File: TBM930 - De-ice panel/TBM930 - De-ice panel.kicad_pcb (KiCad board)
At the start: 2 copper layers, 190.5 x 101.6 mm, 79 parts, among them J1 SW_AIRFRAME_DE_ICE, J10 AVR-ISP-6, J2 SW_ICE_LIGHT, J3 SW_PROP_DE_ICE, J4 SW_WIND_SHIELD, J5 SW_PITOT_L_HTR, J6 SW_PITOT_R_HTR, J7 SW_INERT_SEP, J8 Barrel_Jack, J9 USB_B_Micro, SW1 SW_Push, SW2 SW_Push, U1 TLC5917IN, U2 TLC5917IN, U3 ATmega32U4-MU, Y1 Crystal_GND24

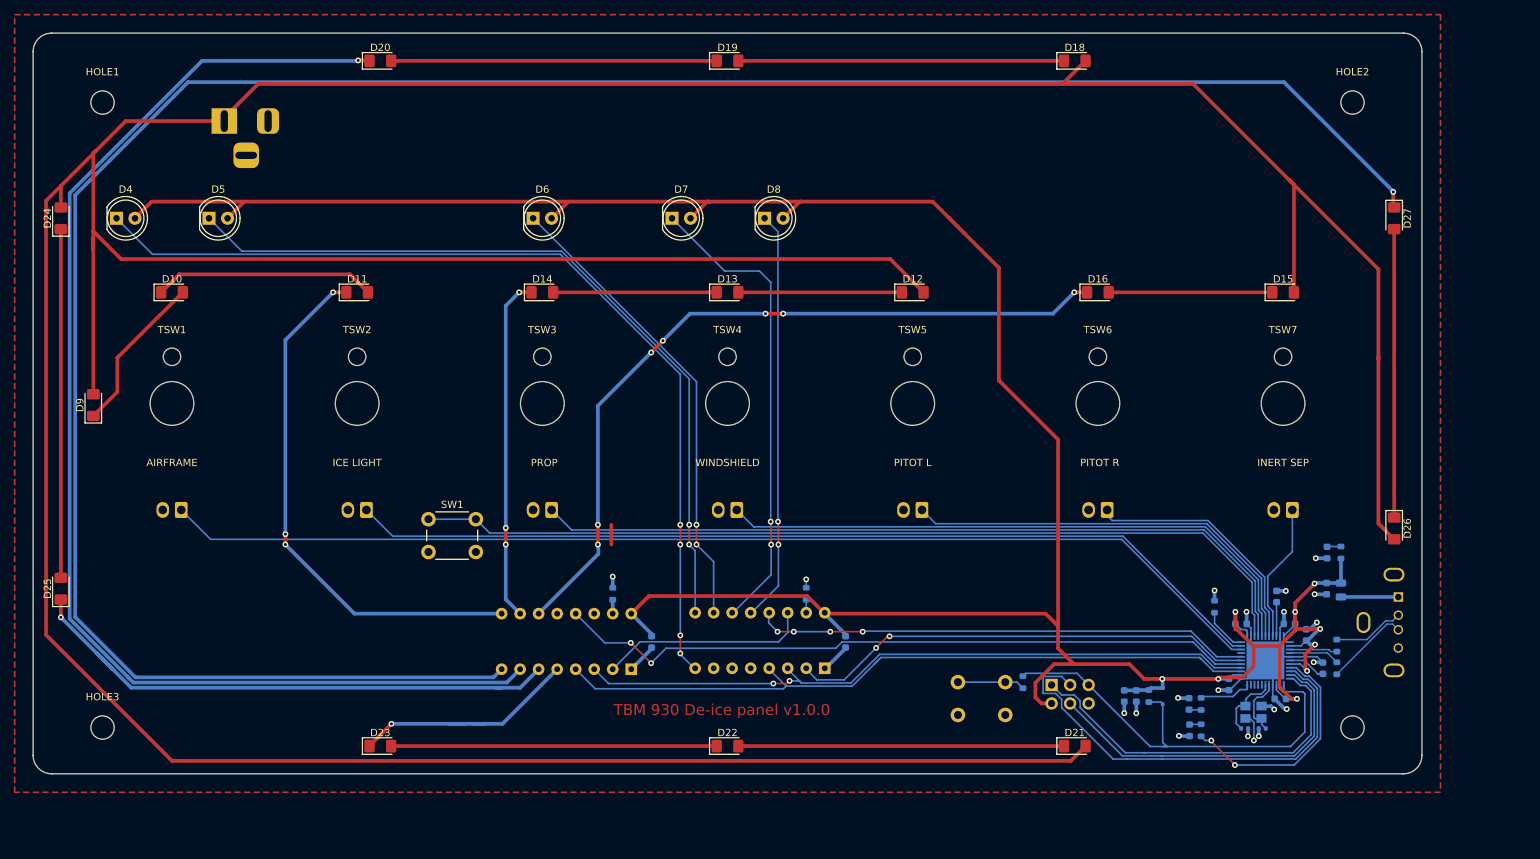
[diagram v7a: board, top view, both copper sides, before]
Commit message: Massive PCB reroute
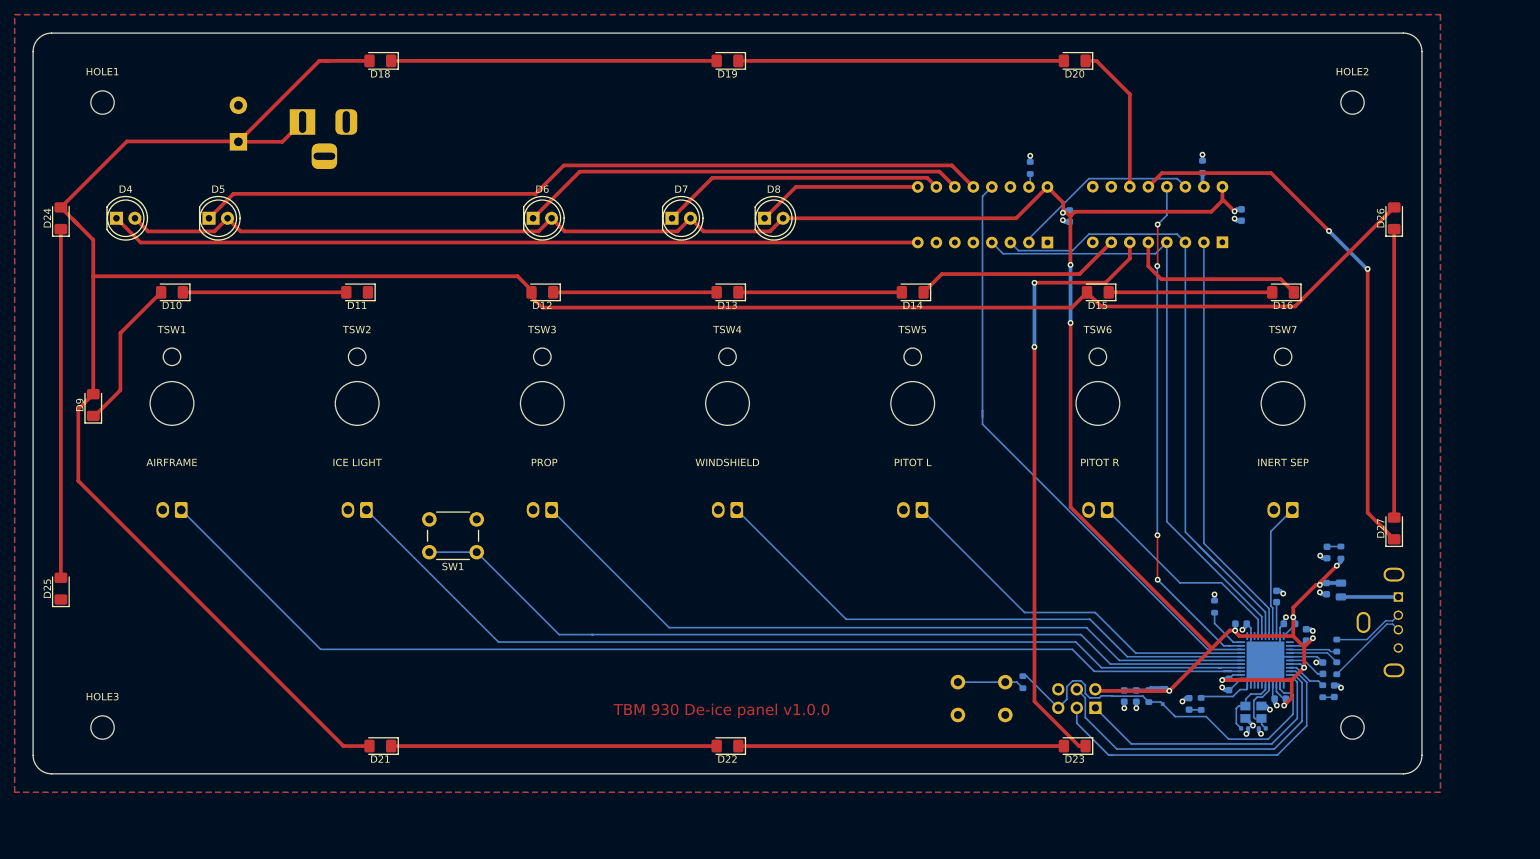
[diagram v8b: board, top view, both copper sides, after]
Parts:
- added J11: Screw_Terminal_01x02, TerminalBlock_Philmore:TerminalBlock_Philmore_TB132_1x02_P5.00mm_Horizontal, B.Cu at (67.5, 57.5)
- moved U1 100.0 mm to (202.5, 71.2)
- moved R4 99.9 mm to (199.8, 60.9)
- moved C8 99.9 mm to (205.1, 67.5)
- moved D18 95.2 mm to (87.0, 46.4), turned to 180 degrees
- moved D20 95.2 mm to (182.2, 46.4), turned to 180 degrees
- moved D21 95.2 mm to (87.0, 140.3), turned to 180 degrees
- moved D23 95.2 mm to (182.2, 140.3), turned to 180 degrees
- moved C9 66.0 mm to (181.5, 67.6)
- moved R3 66.0 mm to (176.1, 61.0)
- moved U2 65.9 mm to (178.5, 71.3)
- moved D12 50.8 mm to (109.2, 78.1), turned to 180 degrees
- moved D14 50.8 mm to (160.0, 78.1), turned to 180 degrees
- moved D26 42.5 mm to (226.1, 67.9), turned to 90 degrees
- moved D27 42.5 mm to (226.1, 110.5), turned to 90 degrees
- moved D15 25.4 mm to (185.4, 78.1), turned to 180 degrees
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- renumbered U2 to U1, U1 to U2
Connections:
- U1 pad 10: BACKLIGHT2 -> BACKLIGHT6
- U1 pad 11: BACKLIGHT3 -> BACKLIGHT4
- U1 pad 12: Net-(U2-Pad12) -> BACKLIGHT7
- U1 pad 14: Net-(U2-Pad14) -> Net-(U1-Pad14)
- U1 pad 2: Net-(U1-Pad14) -> LED_DATA
- U1 pad 5: BACKLIGHT5 -> BACKLIGHT3
- U1 pad 6: BACKLIGHT6 -> BACKLIGHT5
- U1 pad 7: BACKLIGHT4 -> BACKLIGHT2
- U1 pad 8: BACKLIGHT7 -> Net-(U1-Pad8)
- U2 pad 10: PROP -> WINDSHIELD_1
- U2 pad 11: WINDSHIELD_1 -> PROP
- U2 pad 12: WINDSHIELD_2 -> AIRFRAME_2
- U2 pad 14: Net-(U1-Pad14) -> Net-(U2-Pad14)
- U2 pad 2: LED_DATA -> Net-(U1-Pad14)
- U2 pad 9: AIRFRAME_2 -> WINDSHIELD_2
- U3 pad 25: LED_LATCH -> SW_AIRFRAME
- U3 pad 26: LED_CLOCK -> SW_ICE_LIGHT
- U3 pad 27: BACKLIGHT_BRIGHT -> SW_LTS_TEST
- U3 pad 28: LED_DATA -> SW_PROP
- U3 pad 29: INDICATOR_BRIGHT -> SW_WINDSHIELD
- U3 pad 30: /D10 -> SW_PITOT_L
- U3 pad 31: SW_AIRFRAME -> INDICATOR_BRIGHT
- U3 pad 32: SW_ICE_LIGHT -> BACKLIGHT_BRIGHT
- U3 pad 36: SW_LTS_TEST -> /A0
- U3 pad 37: SW_PROP -> SW_PITOT_R
- U3 pad 38: SW_WINDSHIELD -> LED_LATCH
- U3 pad 39: SW_PITOT_L -> LED_CLOCK
- U3 pad 40: SW_PITOT_R -> LED_DATA
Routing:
- net +12V_LED: track 624.6 -> 345.8 mm
- net BACKLIGHT7: track 315.9 -> 74.9 mm, vias 1 -> 2
- net BACKLIGHT4: track 174.0 -> 20.7 mm, vias 1 -> 0
- net BACKLIGHT3: track 105.5 -> 24.7 mm, vias 7 -> 0
- net BACKLIGHT6: track 76.9 -> 0.00 mm, vias 1 -> 0
- net BACKLIGHT1: track 72.7 -> 0.00 mm, vias 3 -> 0
- net BACKLIGHT5: track 33.6 -> 83.6 mm, vias 1 -> 2
- net +5V: track 383.2 -> 339.2 mm, vias 9 -> 13
- net WINDSHIELD_2: track 56.7 -> 22.9 mm, vias 2 -> 0
- net BACKLIGHT_BRIGHT: track 96.6 -> 69.8 mm, vias 2 -> 4
- net /D17: track 31.9 -> 5.51 mm, vias 2 -> 0
- net WINDSHIELD_1: track 64.9 -> 39.1 mm, vias 2 -> 0
- net GND: track 76.8 -> 55.5 mm, vias 20 -> 22
- net BACKLIGHT2: track 47.3 -> 28.6 mm, vias 3 -> 0
- net AIRFRAME_1: track 127.5 -> 111.3 mm, vias 4 -> 0
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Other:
- board text added: "+5V"
- board text added: "GND"
- board text added: "MIOS"
- board text added: "MOSI"
- board text added: "RESET"
- board text added: "SCK"
